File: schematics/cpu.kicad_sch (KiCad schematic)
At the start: 13 parts, among them J1 myBus, SW1 SW_Push, U1 w65c816s

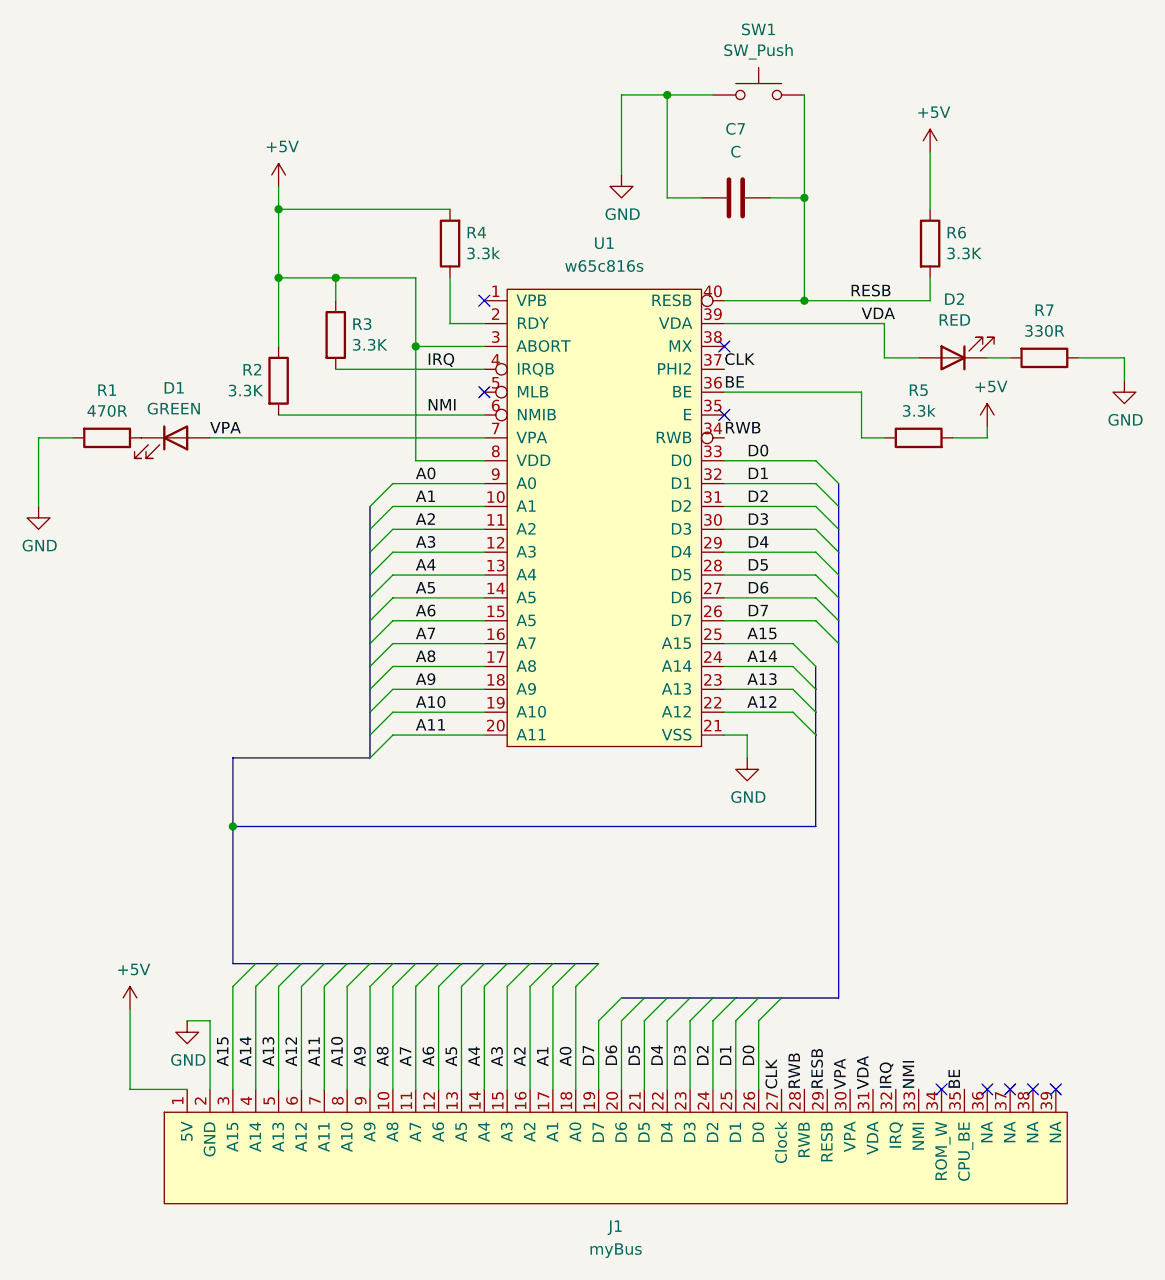
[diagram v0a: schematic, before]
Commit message: Fix errors in schematics
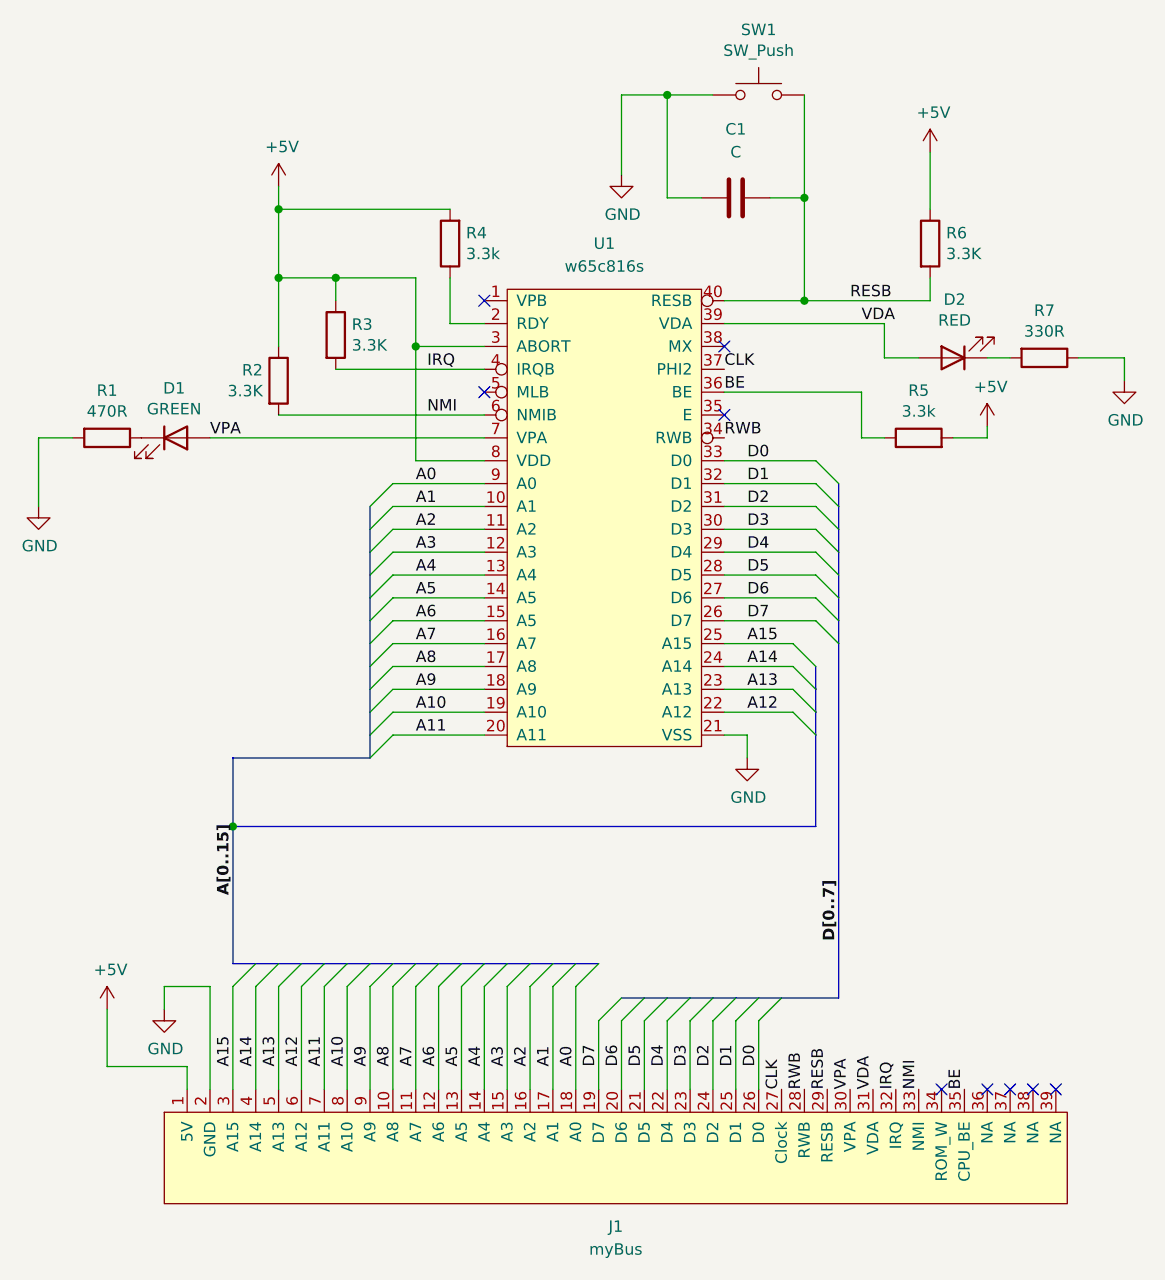
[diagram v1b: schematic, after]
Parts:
- renumbered C7 to C1
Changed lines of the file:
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@@
 	(wire
 		(pts
-			(xy 64.77 146.05) (xy 64.77 138.43)
-		)
-		(stroke
-			(width 0)
-			(type default)
-		)
-	)
-	(wire
-		(pts
 			(xy 118.11 138.43) (xy 118.11 146.05)
 		)
@@
 	(wire
 		(pts
+			(xy 62.23 143.51) (xy 53.34 143.51)
+		)
+		(stroke
+			(width 0)
+			(type default)
+		)
+	)
+	(wire
+		(pts
 			(xy 82.55 146.05) (xy 82.55 134.62)
 		)
@@
 	(wire
 		(pts
+			(xy 59.69 137.16) (xy 59.69 134.62)
+		)
+		(stroke
+			(width 0)
+			(type default)
+		)
+	)
+	(wire
+		(pts
 			(xy 78.74 58.42) (xy 78.74 55.88)
 		)
@@
 	(wire
 		(pts
+			(xy 62.23 146.05) (xy 62.23 143.51)
+		)
+		(stroke
+			(width 0)
+			(type default)
+		)
+	)
+	(wire
+		(pts
 			(xy 69.85 134.62) (xy 69.85 146.05)
 		)
@@
 	(wire
 		(pts
-			(xy 64.77 138.43) (xy 62.23 138.43)
-		)
-		(stroke
-			(width 0)
-			(type default)
-		)
-	)
-	(wire
-		(pts
 			(xy 151.13 73.66) (xy 151.13 72.39)
 		)
@@
 	(wire
 		(pts
+			(xy 53.34 143.51) (xy 53.34 137.16)
+		)
+		(stroke
+			(width 0)
+			(type default)
+		)
+	)
+	(wire
+		(pts
 			(xy 72.39 71.12) (xy 95.25 71.12)
 		)
@@
 		)
 	)
-	(wire
-		(pts
-			(xy 55.88 146.05) (xy 55.88 137.16)
-		)
-		(stroke
-			(width 0)
-			(type default)
-		)
-	)
 	(bus
 		(pts
@@
 	(wire
 		(pts
+			(xy 59.69 134.62) (xy 64.77 134.62)
+		)
+		(stroke
+			(width 0)
+			(type default)
+		)
+	)
+	(wire
+		(pts
 			(xy 95.25 96.52) (xy 85.09 96.52)
 		)
@@
 	(wire
 		(pts
-			(xy 62.23 146.05) (xy 55.88 146.05)
+			(xy 121.92 104.14) (xy 129.54 104.14)
 		)
 		(stroke
@@
 	(wire
 		(pts
-			(xy 121.92 104.14) (xy 129.54 104.14)
+			(xy 87.63 76.2) (xy 87.63 63.5)
 		)
 		(stroke
@@
 	(wire
 		(pts
-			(xy 87.63 76.2) (xy 87.63 63.5)
+			(xy 130.81 35.56) (xy 130.81 46.99)
 		)
 		(stroke
@@
 		)
 	)
-	(wire
+	(bus
 		(pts
-			(xy 130.81 35.56) (xy 130.81 46.99)
+			(xy 82.55 104.14) (xy 82.55 106.68)
 		)
 		(stroke
@@
 	(bus
 		(pts
-			(xy 82.55 104.14) (xy 82.55 106.68)
+			(xy 134.62 81.28) (xy 134.62 83.82)
 		)
 		(stroke
@@
 		)
 	)
-	(bus
+	(wire
 		(pts
-			(xy 134.62 81.28) (xy 134.62 83.82)
+			(xy 64.77 134.62) (xy 64.77 146.05)
 		)
 		(stroke
@@
 		)
 	)
+	(label "A[0..15]"
+		(at 67.31 124.46 90)
+		(fields_autoplaced yes)
+		(effects
+			(font
+				(size 1.27 1.27)
+				(bold yes)
+			)
+			(justify left bottom)
+		)
+	)
 	(label "NMI"
 		(at 88.9 71.12 0)
@@
 		)
 	)
+	(label "D[0..7]"
+		(at 134.62 129.54 90)
+		(fields_autoplaced yes)
+		(effects
+			(font
+				(size 1.27 1.27)
+				(bold yes)
+			)
+			(justify left bottom)
+		)
+	)
 	(label "IRQ"
 		(at 140.97 146.05 90)
@@
 	)
 	(symbol
-		(lib_id "Device:R")
-		(at 53.34 73.66 270)
+		(lib_id "power:GND")
+		(at 59.69 137.16 0)
 		(unit 1)
 		(exclude_from_sim no)
@@
 		(on_board yes)
 		(dnp no)
-		(property "Reference" "R1"
-			(at 53.34 68.4022 90)
+		(property "Reference" "#PWR05"
+			(at 59.69 143.51 0)
 			(effects
 				(font
 					(size 1.27 1.27)
 				)
+				(hide yes)
 			)
 		)
-		(property "Value" "470R"
-			(at 53.34 70.7136 90)
+		(property "Value" "GND"
+			(at 59.817 141.5542 0)
 			(effects
 				(font
@@
 		)
 		(property "Footprint" ""
-			(at 53.34 71.882 90)
+			(at 59.69 137.16 0)
 			(effects
 				(font
@@
 			)
 		)
-		(property "Datasheet" "~"
-			(at 53.34 73.66 0)
+		(property "Datasheet" ""
+			(at 59.69 137.16 0)
 			(effects
 				(font
@@
 			)
 		)
-		(property "Description" "Resistor"
-			(at 53.34 73.66 0)
+		(property "Description" "Power symbol creates a global label with name \"GND\" , ground"
+			(at 59.69 137.16 0)
 			(effects
 				(font
@@
 			)
 		)
-		(pin "2"
-		)
 		(pin "1"
 		)
@@
 			(project "markus"
 				(path "/03a78ca6-eaff-4f05-be7b-36cd15f8b56d/000b9081-868b-4dc4-bc32-6aa9fd761f74"
-					(reference "R1")
+					(reference "#PWR05")
 					(unit 1)
 				)
@@
 	)
 	(symbol
-		(lib_id "power:+5V")
-		(at 55.88 137.16 0)
+		(lib_id "Device:R")
+		(at 53.34 73.66 270)
 		(unit 1)
 		(exclude_from_sim no)
@@
 		(on_board yes)
 		(dnp no)
-		(property "Reference" "#PWR04"
-			(at 55.88 140.97 0)
+		(property "Reference" "R1"
+			(at 53.34 68.4022 90)
 			(effects
 				(font
 					(size 1.27 1.27)
 				)
-				(hide yes)
 			)
 		)
-		(property "Value" "+5V"
-			(at 56.261 132.7658 0)
+		(property "Value" "470R"
+			(at 53.34 70.7136 90)
 			(effects
 				(font
@@
 		)
 		(property "Footprint" ""
-			(at 55.88 137.16 0)
+			(at 53.34 71.882 90)
 			(effects
 				(font
@@
 			)
 		)
-		(property "Datasheet" ""
-			(at 55.88 137.16 0)
+		(property "Datasheet" "~"
+			(at 53.34 73.66 0)
 			(effects
 				(font
@@
 			)
 		)
-		(property "Description" "Power symbol creates a global label with name \"+5V\""
-			(at 55.88 137.16 0)
+		(property "Description" "Resistor"
+			(at 53.34 73.66 0)
 			(effects
 				(font
@@
 			)
 		)
+		(pin "2"
+		)
 		(pin "1"
 		)
@@
 			(project "markus"
 				(path "/03a78ca6-eaff-4f05-be7b-36cd15f8b56d/000b9081-868b-4dc4-bc32-6aa9fd761f74"
-					(reference "#PWR04")
+					(reference "R1")
 					(unit 1)
 				)
@@
 	)
 	(symbol
-		(lib_id "power:GND")
-		(at 62.23 138.43 0)
+		(lib_id "power:+5V")
+		(at 53.34 137.16 0)
 		(unit 1)
 		(exclude_from_sim no)
@@
 		(on_board yes)
 		(dnp no)
-		(property "Reference" "#PWR05"
-			(at 62.23 144.78 0)
+		(property "Reference" "#PWR04"
+			(at 53.34 140.97 0)
 			(effects
 				(font
@@
 			)
 		)
-		(property "Value" "GND"
-			(at 62.357 142.8242 0)
+		(property "Value" "+5V"
+			(at 53.721 132.7658 0)
 			(effects
 				(font
@@
 		)
 		(property "Footprint" ""
-			(at 62.23 138.43 0)
+			(at 53.34 137.16 0)
 			(effects
 				(font
@@
 		)
 		(property "Datasheet" ""
-			(at 62.23 138.43 0)
+			(at 53.34 137.16 0)
 			(effects
 				(font
@@
 			)
 		)
-		(property "Description" "Power symbol creates a global label with name \"GND\" , ground"
-			(at 62.23 138.43 0)
+		(property "Description" "Power symbol creates a global label with name \"+5V\""
+			(at 53.34 137.16 0)
 			(effects
 				(font
@@
 			(project "markus"
 				(path "/03a78ca6-eaff-4f05-be7b-36cd15f8b56d/000b9081-868b-4dc4-bc32-6aa9fd761f74"
-					(reference "#PWR05")
+					(reference "#PWR04")
 					(unit 1)
 				)
@@
 		(dnp no)
 		(fields_autoplaced yes)
-		(property "Reference" "C7"
+		(property "Reference" "C1"
 			(at 123.19 39.37 90)
 			(effects
@@
 			(project ""
 				(path "/03a78ca6-eaff-4f05-be7b-36cd15f8b56d/000b9081-868b-4dc4-bc32-6aa9fd761f74"
-					(reference "C7")
+					(reference "C1")
 					(unit 1)
 				)

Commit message: Update ROM design
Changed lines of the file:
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@@
 	(label "A6"
 		(at 87.63 93.98 0)
-		(fields_autoplaced yes)
 		(effects
 			(font
@@
 	(label "A11"
 		(at 87.63 106.68 0)
-		(fields_autoplaced yes)
 		(effects
 			(font
@@
 	(label "A10"
 		(at 80.01 143.51 90)
-		(fields_autoplaced yes)
 		(effects
 			(font
@@
 	(label "A15"
 		(at 124.46 96.52 0)
-		(fields_autoplaced yes)
 		(effects
 			(font
@@
 	(label "IRQ"
 		(at 88.9 66.04 0)
-		(fields_autoplaced yes)
 		(effects
 			(font
@@
 	(label "A12"
 		(at 74.93 143.51 90)
-		(fields_autoplaced yes)
 		(effects
 			(font
@@
 	(label "D6"
 		(at 110.49 143.51 90)
-		(fields_autoplaced yes)
 		(effects
 			(font
@@
 	(label "A9"
 		(at 87.63 101.6 0)
-		(fields_autoplaced yes)
 		(effects
 			(font
@@
 	(label "A0"
 		(at 87.63 78.74 0)
-		(fields_autoplaced yes)
 		(effects
 			(font
@@
 	(label "A5"
 		(at 92.71 143.51 90)
-		(fields_autoplaced yes)
 		(effects
 			(font
@@
 	(label "A4"
 		(at 87.63 88.9 0)
-		(fields_autoplaced yes)
 		(effects
 			(font
@@
 	(label "A10"
 		(at 87.63 104.14 0)
-		(fields_autoplaced yes)
 		(effects
 			(font
@@
 	(label "D3"
 		(at 124.46 83.82 0)
-		(fields_autoplaced yes)
 		(effects
 			(font
@@
 	(label "VPA"
 		(at 64.77 73.66 0)
-		(fields_autoplaced yes)
 		(effects
 			(font
@@
 	(label "A15"
 		(at 67.31 143.51 90)
-		(fields_autoplaced yes)
 		(effects
 			(font
@@
 	(label "A7"
 		(at 87.63 96.52 0)
-		(fields_autoplaced yes)
 		(effects
 			(font
@@
 	(label "RWB"
 		(at 121.92 73.66 0)
-		(fields_autoplaced yes)
 		(effects
 			(font
@@
 	(label "D1"
 		(at 124.46 78.74 0)
-		(fields_autoplaced yes)
 		(effects
 			(font
@@
 	(label "BE"
 		(at 121.92 68.58 0)
-		(fields_autoplaced yes)
 		(effects
 			(font
@@
 	(label "A[0..15]"
 		(at 67.31 124.46 90)
-		(fields_autoplaced yes)
 		(effects
 			(font
@@
 	(label "NMI"
 		(at 88.9 71.12 0)
-		(fields_autoplaced yes)
 		(effects
 			(font
@@
 	(label "D3"
 		(at 118.11 143.51 90)
-		(fields_autoplaced yes)
 		(effects
 			(font
@@
 	(label "A0"
 		(at 105.41 143.51 90)
-		(fields_autoplaced yes)
 		(effects
 			(font
@@
 	(label "A7"
 		(at 87.63 143.51 90)
-		(fields_autoplaced yes)
 		(effects
 			(font
@@
 	(label "A8"
 		(at 87.63 99.06 0)
-		(fields_autoplaced yes)
 		(effects
 			(font
@@
 	(label "NMI"
 		(at 143.51 146.05 90)
-		(fields_autoplaced yes)
 		(effects
 			(font
@@
 	(label "A1"
 		(at 87.63 81.28 0)
-		(fields_autoplaced yes)
 		(effects
 			(font
@@
 	(label "D7"
 		(at 107.95 143.51 90)
-		(fields_autoplaced yes)
 		(effects
 			(font
@@
 	(label "RWB"
 		(at 130.81 146.05 90)
-		(fields_autoplaced yes)
 		(effects
 			(font
@@
 	(label "A2"
 		(at 100.33 143.51 90)
-		(fields_autoplaced yes)
 		(effects
 			(font
@@
 	(label "RESB"
 		(at 133.35 146.05 90)
-		(fields_autoplaced yes)
 		(effects
 			(font
@@
 	(label "VPA"
 		(at 135.89 146.05 90)
-		(fields_autoplaced yes)
 		(effects
 			(font
@@
 	(label "D1"
 		(at 123.19 143.51 90)
-		(fields_autoplaced yes)
 		(effects
 			(font
@@
 	(label "CLK"
 		(at 121.92 66.04 0)
-		(fields_autoplaced yes)
 		(effects
 			(font
@@
 	(label "D6"
 		(at 124.46 91.44 0)
-		(fields_autoplaced yes)
 		(effects
 			(font
@@
 	(label "A9"
 		(at 82.55 143.51 90)
-		(fields_autoplaced yes)
 		(effects
 			(font
@@
 	(label "A3"
 		(at 87.63 86.36 0)
-		(fields_autoplaced yes)
 		(effects
 			(font
@@
 	(label "D2"
 		(at 120.65 143.51 90)
-		(fields_autoplaced yes)
 		(effects
 			(font
@@
 	(label "A14"
 		(at 69.85 143.51 90)
-		(fields_autoplaced yes)
 		(effects
 			(font
@@
 	(label "RESB"
 		(at 135.89 58.42 0)
-		(fields_autoplaced yes)
 		(effects
 			(font
@@
 	(label "A4"
 		(at 95.25 143.51 90)
-		(fields_autoplaced yes)
 		(effects
 			(font
@@
 	(label "D2"
 		(at 124.46 81.28 0)
-		(fields_autoplaced yes)
 		(effects
 			(font
@@
 	(label "A2"
 		(at 87.63 83.82 0)
-		(fields_autoplaced yes)
 		(effects
 			(font
@@
 	(label "A14"
 		(at 124.46 99.06 0)
-		(fields_autoplaced yes)
 		(effects
 			(font
@@
 	(label "D5"
 		(at 113.03 143.51 90)
-		(fields_autoplaced yes)
 		(effects
 			(font
@@
 	(label "A8"
 		(at 85.09 143.51 90)
-		(fields_autoplaced yes)
 		(effects
 			(font
@@
 	(label "D7"
 		(at 124.46 93.98 0)
-		(fields_autoplaced yes)
 		(effects
 			(font
@@
 	(label "D4"
 		(at 115.57 143.51 90)
-		(fields_autoplaced yes)
 		(effects
 			(font
@@
 	(label "D[0..7]"
 		(at 134.62 129.54 90)
-		(fields_autoplaced yes)
 		(effects
 			(font
@@
 	(label "IRQ"
 		(at 140.97 146.05 90)
-		(fields_autoplaced yes)
 		(effects
 			(font
@@
 	(label "D4"
 		(at 124.46 86.36 0)
-		(fields_autoplaced yes)
 		(effects
 			(font
@@
 	(label "A13"
 		(at 124.46 101.6 0)
-		(fields_autoplaced yes)
 		(effects
 			(font
@@
 	(label "A6"
 		(at 90.17 143.51 90)
-		(fields_autoplaced yes)
 		(effects
 			(font
@@
 	(label "D0"
 		(at 124.46 76.2 0)
-		(fields_autoplaced yes)
 		(effects
 			(font
@@
 	(label "BE"
 		(at 148.59 146.05 90)
-		(fields_autoplaced yes)
 		(effects
 			(font
@@
 	(label "A3"
 		(at 97.79 143.51 90)
-		(fields_autoplaced yes)
 		(effects
 			(font
@@
 	(label "A1"
 		(at 102.87 143.51 90)
-		(fields_autoplaced yes)
 		(effects
 			(font
@@
 	(label "A13"
 		(at 72.39 143.51 90)
-		(fields_autoplaced yes)
 		(effects
 			(font
@@
 	(label "A5"
 		(at 87.63 91.44 0)
-		(fields_autoplaced yes)
 		(effects
 			(font
@@
 	(label "D0"
 		(at 125.73 143.51 90)
-		(fields_autoplaced yes)
 		(effects
 			(font
@@
 	(label "A11"
 		(at 77.47 143.51 90)
-		(fields_autoplaced yes)
 		(effects
 			(font
@@
 	(label "D5"
 		(at 124.46 88.9 0)
-		(fields_autoplaced yes)
 		(effects
 			(font
@@
 	(label "VDA"
 		(at 138.43 146.05 90)
-		(fields_autoplaced yes)
 		(effects
 			(font
@@
 	(label "A12"
 		(at 124.46 104.14 0)
-		(fields_autoplaced yes)
 		(effects
 			(font
@@
 	(label "CLK"
 		(at 128.27 146.05 90)
-		(fields_autoplaced yes)
 		(effects
 			(font
@@
 	(label "VDA"
 		(at 137.16 60.96 0)
-		(fields_autoplaced yes)
-		(effects
-			(font
+		(effects
+			(font
